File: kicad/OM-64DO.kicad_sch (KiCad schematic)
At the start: 27 parts, among them J101 15EDGVC-3.5-4P, J102 02x03 1.27, J201 15EDGVC-3.5-20P, J301 15EDGVC-3.5-20P, J401 15EDGVC-3.5-20P, J501 15EDGVC-3.5-20P, U101 R-78E3.3-1.0, U102 THVD1450DRBR, U103 STM32G031F8P6

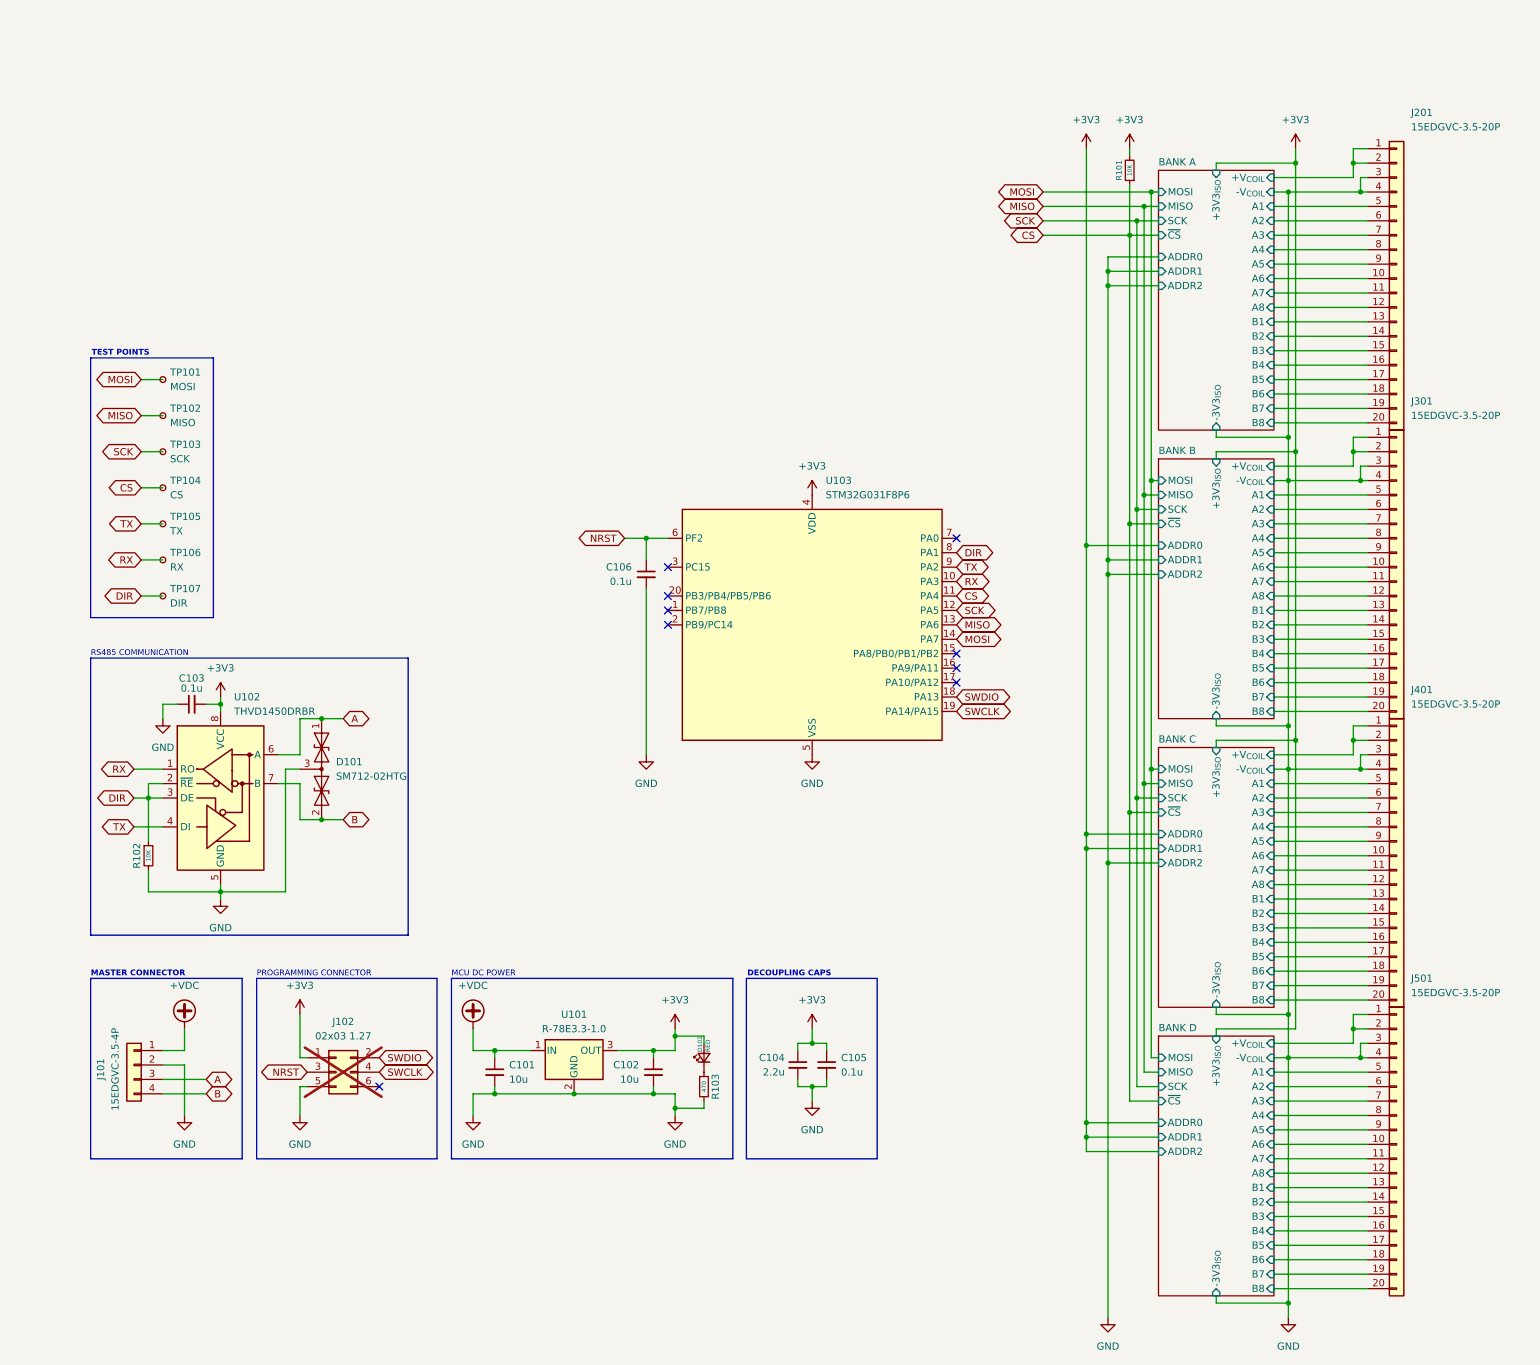
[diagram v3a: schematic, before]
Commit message: feat: add extra power rail protection
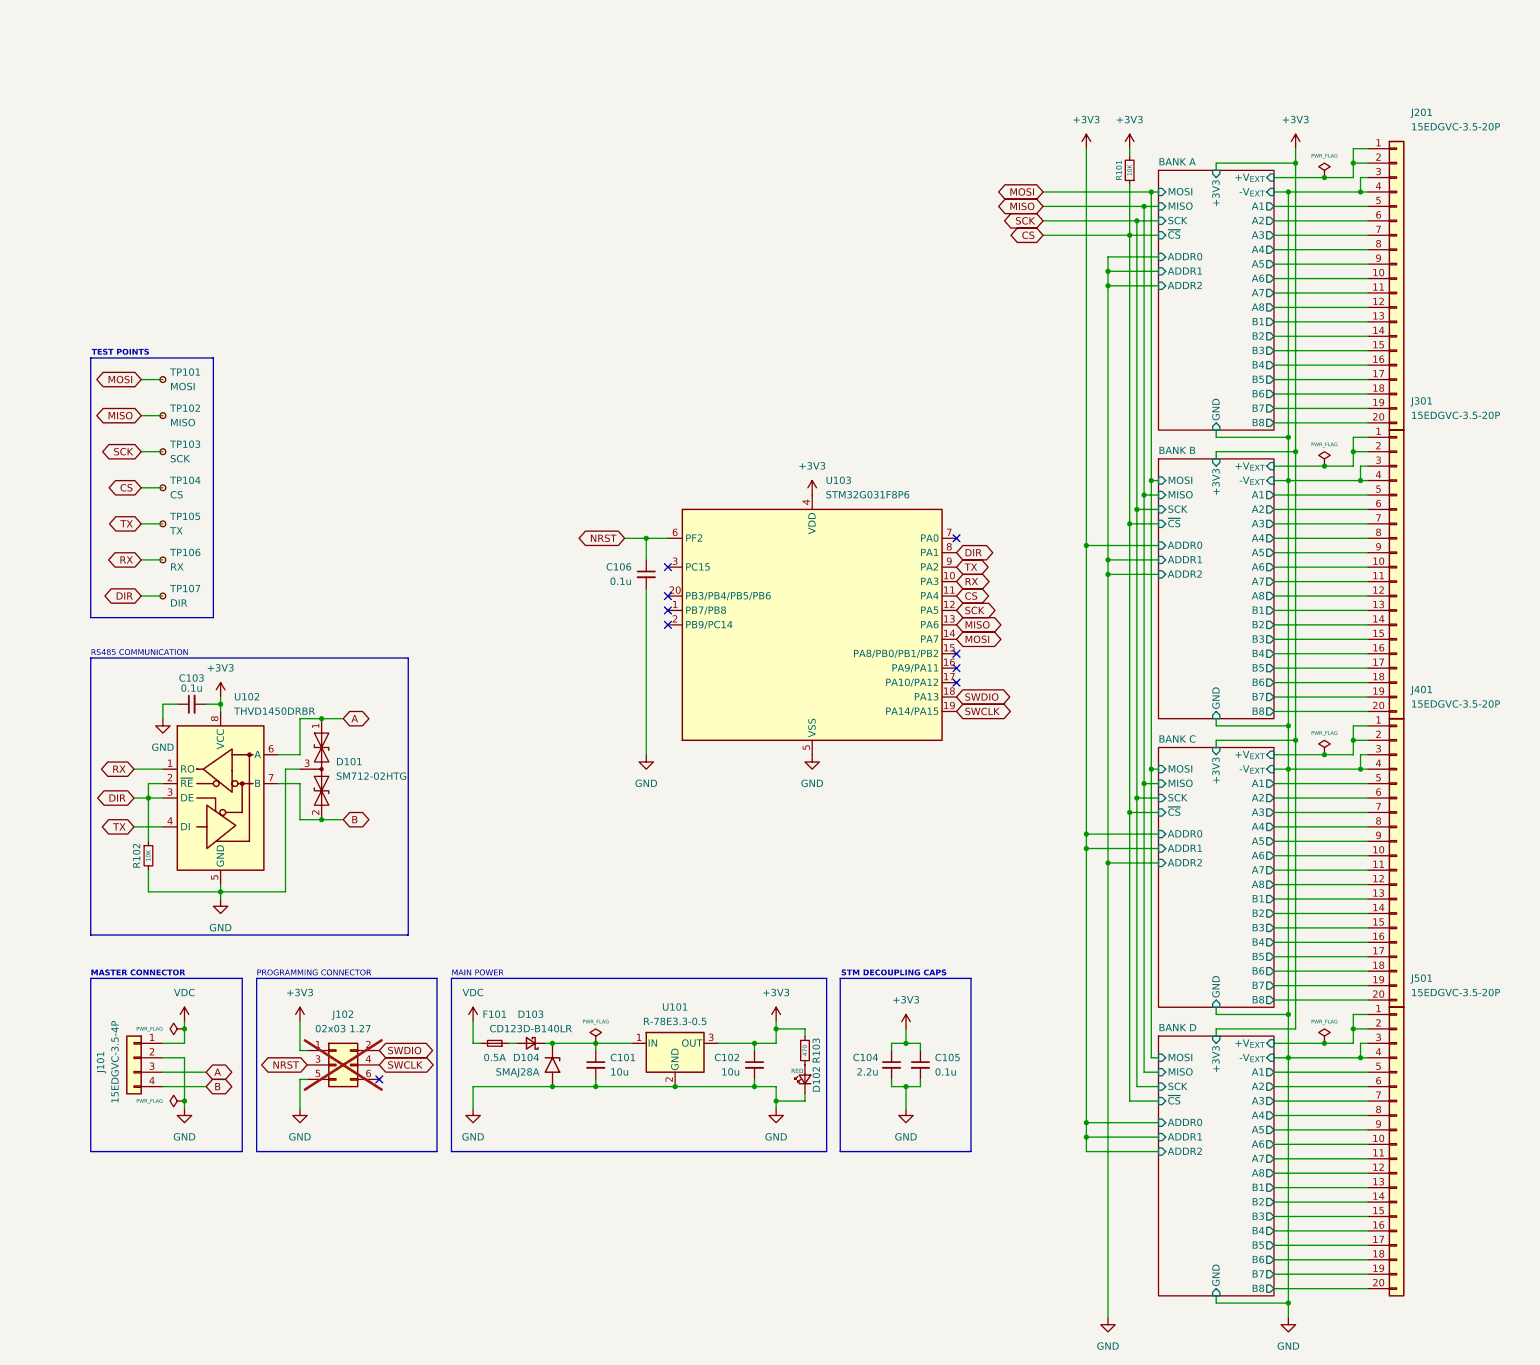
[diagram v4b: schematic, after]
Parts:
- added D103: CD123D-B140LR, Diode_SMD:D_SOD-123, symbol Device:D_Schottky_Small
- added D104: SMAJ28A, Diode_SMD:D_SMA, symbol Diode:SMAJ28A
- added F101: 0.5A, Fuse:Fuse_1206_3216Metric, symbol Device:Fuse_Small
- U101: value R-78E3.3-1.0 -> R-78E3.3-0.5; Mouser Part Number 919-R-78E3.3-1.0 -> 919-R-78E3.3-0.5; Part Number R-78E3.3-1.0 -> R-78E3.3-0.5
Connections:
- net +3V3: now also R103.1; no longer D102.2 (A)
- net GND: now also D102.1 (K), D104.2 (A2); no longer R103.2
- net +VDC: no longer names the net of C101.1, U101.1 (IN)
- net +VDC: now also D103.1 (K), D104.1 (A1); no longer J101.1 (Pin_1)
- net BANK A/+V_{COIL} renamed BANK A/+V_{EXT}
- net BANK B/+V_{COIL} renamed BANK B/+V_{EXT}
- net BANK C/+V_{COIL} renamed BANK C/+V_{EXT}
- net BANK D/+V_{COIL} renamed BANK D/+V_{EXT}
- new net: D102.2 (A), R103.2
- new net: D103.2 (A), F101.1
- new net VDC: F101.2, J101.1 (Pin_1)
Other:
- sheet BANK A ports: added +3V3, +V_{EXT}, -V_{EXT}, GND; removed +3V3_{ISO}, +V_{COIL}, -3V3_{ISO}, -V_{COIL}
- sheet BANK B ports: added +3V3, +V_{EXT}, -V_{EXT}, GND; removed +3V3_{ISO}, +V_{COIL}, -3V3_{ISO}, -V_{COIL}
- sheet BANK C ports: added +3V3, +V_{EXT}, -V_{EXT}, GND; removed +3V3_{ISO}, +V_{COIL}, -3V3_{ISO}, -V_{COIL}
- sheet BANK D ports: added +3V3, +V_{EXT}, -V_{EXT}, GND; removed +3V3_{ISO}, +V_{COIL}, -3V3_{ISO}, -V_{COIL}
- note added: "MAIN POWER"
- note added: "STM DECOUPLING CAPS"
- note removed: "DECOUPLING CAPS"
- note removed: "MCU DC POWER"
- moved on the sheet: C101, C102, C104, C105, D102, J101, J102, R103, U101
